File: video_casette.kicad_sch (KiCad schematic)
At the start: 4 parts, among them Q2 1402D, Q3 1402D

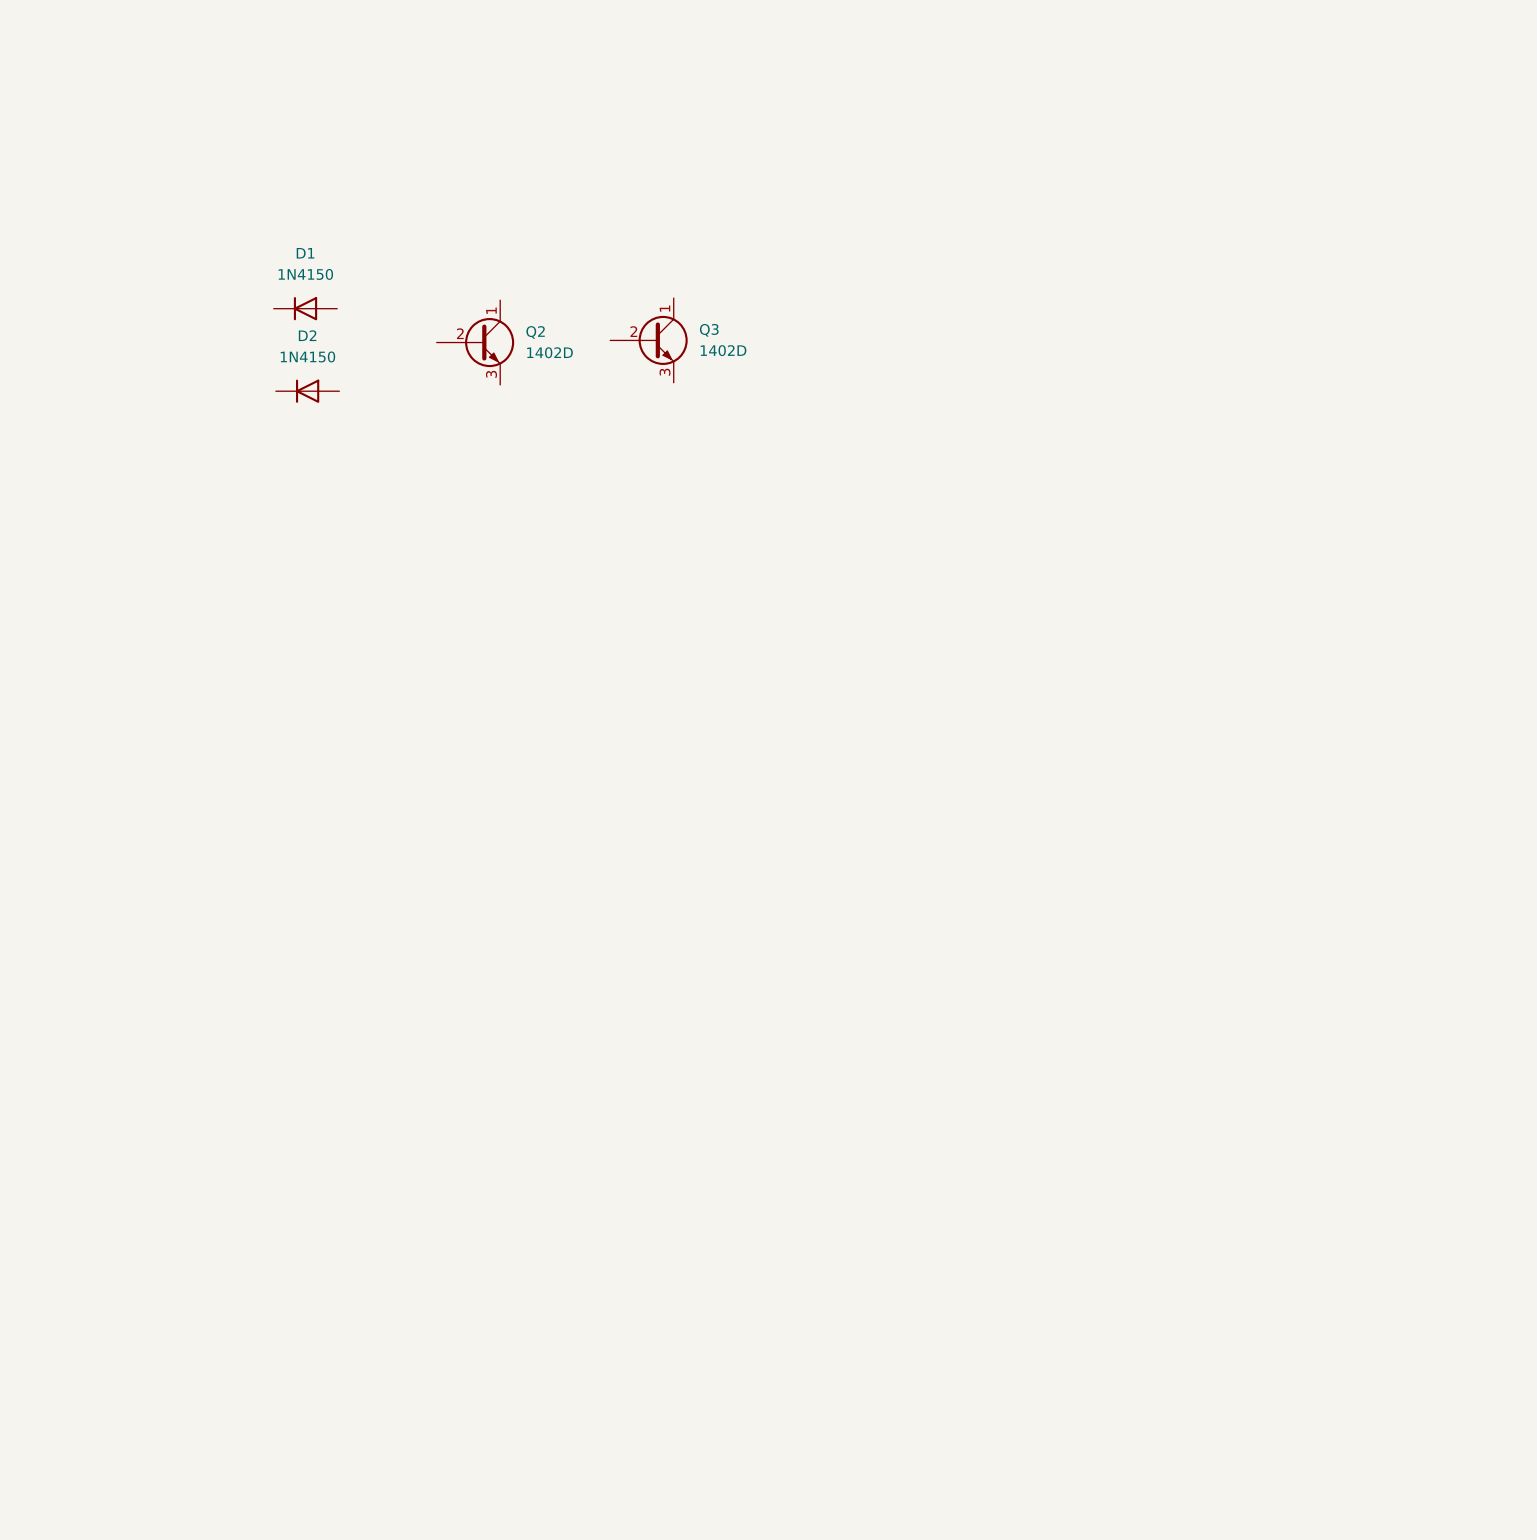
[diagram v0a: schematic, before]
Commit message: Finished Y-signal generation
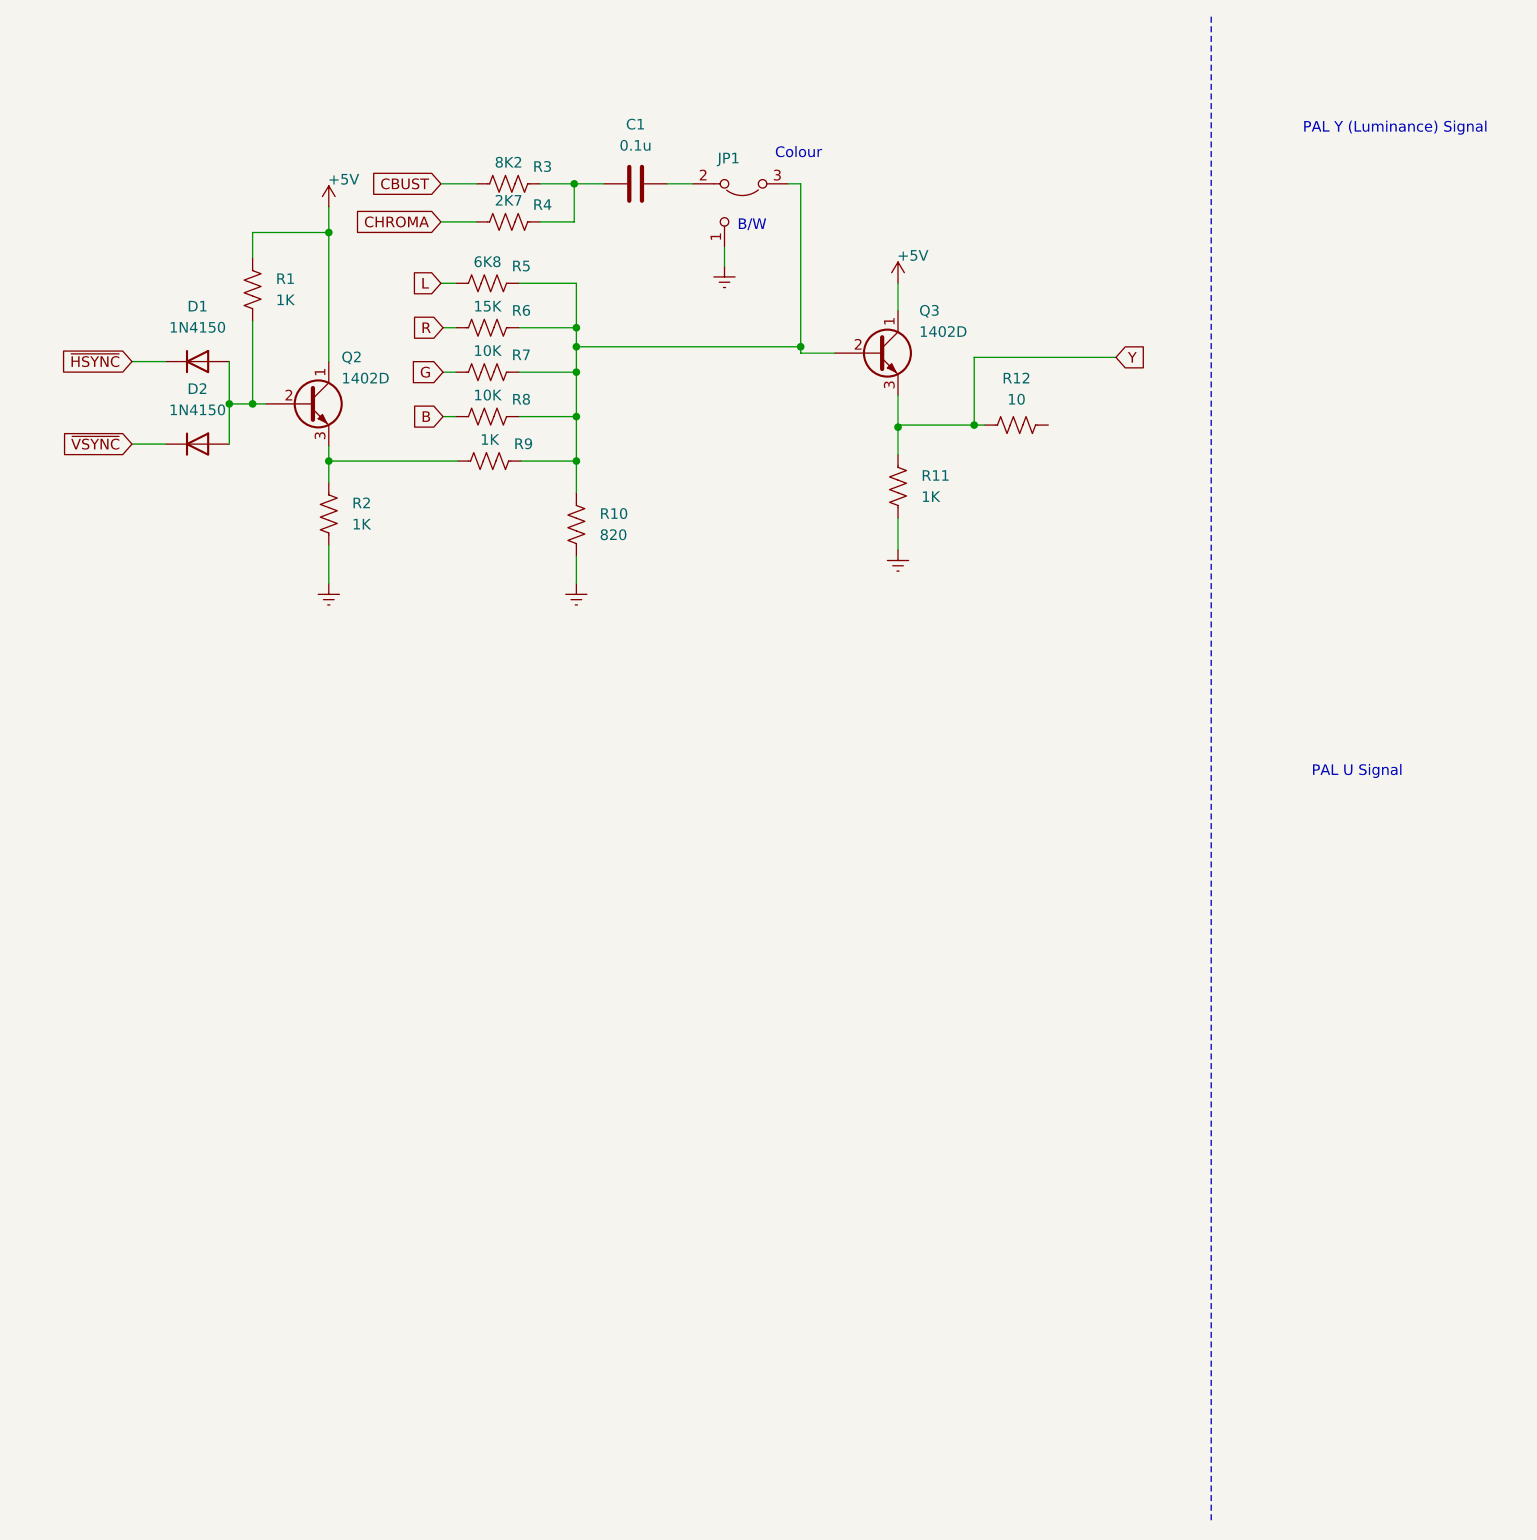
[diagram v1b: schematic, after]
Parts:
- added C1: 0.1u, symbol Device:C
- added JP1: Jumper 2-to-1_Bridged_23, symbol Laser500:Jumper 1-to-2
- added R1, R11, R2, R9: 1K, Resistor_THT:R_Axial_DIN0207_L6.3mm_D2.5mm_P7.62mm_Horizontal, symbol Device:R_US
- added R10: 820, Resistor_THT:R_Axial_DIN0207_L6.3mm_D2.5mm_P7.62mm_Horizontal, symbol Device:R_US
- added R12: 10, Resistor_THT:R_Axial_DIN0207_L6.3mm_D2.5mm_P7.62mm_Horizontal, symbol Device:R_US
- added R3: 8K2, Resistor_THT:R_Axial_DIN0207_L6.3mm_D2.5mm_P7.62mm_Horizontal, symbol Device:R_US
- added R4: 2K7, Resistor_THT:R_Axial_DIN0207_L6.3mm_D2.5mm_P7.62mm_Horizontal, symbol Device:R_US
- added R5: 6K8, Resistor_THT:R_Axial_DIN0207_L6.3mm_D2.5mm_P7.62mm_Horizontal, symbol Device:R_US
- added R6: 15K, Resistor_THT:R_Axial_DIN0207_L6.3mm_D2.5mm_P7.62mm_Horizontal, symbol Device:R_US
- added R7, R8: 10K, Resistor_THT:R_Axial_DIN0207_L6.3mm_D2.5mm_P7.62mm_Horizontal, symbol Device:R_US
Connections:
- net ~{HSYNC}: now reaches D1.1 (K)
- net at D1.2 (A): now also D2.2 (A), Q2.2 (B), R1.2
- net +5V: now reaches Q3.1 (C)
- net +5V: now also Q2.1 (C), R1.1
- net at Q3.2 (B): now also JP1.3 (B), R10.1, R5.1, R6.1, R7.1, R8.1, R9.1
- net Y: now reaches Q3.3 (E)
- net Y: now also R11.1, R12.1
- net ~{VSYNC}: now reaches D2.1 (K)
- net at Q2.3 (E): now also R2.1, R9.2
- new net: C1.2, R3.1, R4.1
- new net: C1.1, JP1.2 (C)
- new net B: R8.2
- new net CBUST: R3.2
- new net CHROMA: R4.2
- new net G: R7.2
- new net L: R5.2
- new net R: R6.2
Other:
- note added: "B/W"
- note added: "Colour"
- note added: "PAL U Signal"
- note added: "PAL Y (Luminance) Signal"
- moved on the sheet: D1, D2, Q2, Q3

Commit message: End of vacation
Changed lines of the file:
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@@
-		)
-	)
-	(global_label "R"
-		(shape input)
-		(at 60.452 52.07 180)
-		(fields_autoplaced yes)
-		(effects
-			(font
-				(size 1.27 1.27)
-			)
-			(justify right)
-		)
-		(property "Intersheetrefs" "${INTERSHEET_REFS}"
-			(at 56.1968 52.07 0)
-			(effects
-				(font
-					(size 1.27 1.27)
-				)
-				(justify right)
-				(hide yes)
-			)
 		)
 	)
@@
 		)
 	)
-	(global_label "B"
-		(shape input)
-		(at 60.452 62.738 180)
-		(fields_autoplaced yes)
-		(effects
-			(font
-				(size 1.27 1.27)
-			)
-			(justify right)
-		)
-		(property "Intersheetrefs" "${INTERSHEET_REFS}"
-			(at 56.1968 62.738 0)
-			(effects
-				(font
-					(size 1.27 1.27)
-				)
-				(justify right)
-				(hide yes)
-			)
-		)
-	)
-	(global_label "G"
-		(shape input)
-		(at 60.452 57.404 180)
-		(fields_autoplaced yes)
-		(effects
-			(font
-				(size 1.27 1.27)
-			)
-			(justify right)
-		)
-		(property "Intersheetrefs" "${INTERSHEET_REFS}"
-			(at 56.1968 57.404 0)
-			(effects
-				(font
-					(size 1.27 1.27)
-				)
-				(justify right)
-				(hide yes)
-			)
-		)
-	)
 	(global_label "~{HSYNC}"
 		(shape input)
@@
 		(property "Intersheetrefs" "${INTERSHEET_REFS}"
 			(at 13.8997 56.134 0)
-			(effects
-				(font
-					(size 1.27 1.27)
-				)
-				(justify right)
-				(hide yes)
-			)
-		)
-	)
-	(global_label "L"
-		(shape input)
-		(at 60.198 46.736 180)
-		(fields_autoplaced yes)
-		(effects
-			(font
-				(size 1.27 1.27)
-			)
-			(justify right)
-		)
-		(property "Intersheetrefs" "${INTERSHEET_REFS}"
-			(at 56.1847 46.736 0)
 			(effects
 				(font
@@
 		)
 	)
+	(hierarchical_label "R"
+		(shape input)
+		(at 60.452 52.07 180)
+		(fields_autoplaced yes)
+		(effects
+			(font
+				(size 1.27 1.27)
+			)
+			(justify right)
+		)
+	)
+	(hierarchical_label "B"
+		(shape input)
+		(at 60.452 62.738 180)
+		(fields_autoplaced yes)
+		(effects
+			(font
+				(size 1.27 1.27)
+			)
+			(justify right)
+		)
+	)
+	(hierarchical_label "G"
+		(shape input)
+		(at 60.452 57.404 180)
+		(fields_autoplaced yes)
+		(effects
+			(font
+				(size 1.27 1.27)
+			)
+			(justify right)
+		)
+	)
+	(hierarchical_label "L"
+		(shape input)
+		(at 60.198 46.736 180)
+		(fields_autoplaced yes)
+		(effects
+			(font
+				(size 1.27 1.27)
+			)
+			(justify right)
+		)
+	)

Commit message: More updates on Top and Main diagrams
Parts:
- added R??: 10K, Resistor_THT:R_Axial_DIN0207_L6.3mm_D2.5mm_P7.62mm_Horizontal, symbol Device:R_US
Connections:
- new net CASOUT: R??.2
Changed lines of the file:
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@@
+	(wire
+		(pts
+			(xy 34.29 111.76) (xy 41.91 111.76)
+		)
+		(stroke
+			(width 0)
+			(type default)
+		)
+	)
 	(wire
 		(pts
@@
 		)
 	)
-	(global_label "~{VSYNC}"
+	(global_label "Y"
 		(shape input)
-		(at 23.114 66.04 180)
+		(at 141.224 55.626 0)
 		(fields_autoplaced yes)
 		(effects
@@
 				(size 1.27 1.27)
 			)
-			(justify right)
+			(justify left)
 		)
 		(property "Intersheetrefs" "${INTERSHEET_REFS}"
-			(at 14.1416 66.04 0)
-			(effects
-				(font
-					(size 1.27 1.27)
-				)
-				(justify right)
-				(hide yes)
-			)
-		)
-	)
-	(global_label "CHROMA"
+			(at 145.2978 55.626 0)
+			(effects
+				(font
+					(size 1.27 1.27)
+				)
+				(justify left)
+				(hide yes)
+			)
+		)
+	)
+	(hierarchical_label "R"
 		(shape input)
-		(at 60.198 39.37 180)
+		(at 60.452 52.07 180)
 		(fields_autoplaced yes)
 		(effects
@@
 			(justify right)
 		)
-		(property "Intersheetrefs" "${INTERSHEET_REFS}"
-			(at 49.4718 39.37 0)
-			(effects
-				(font
-					(size 1.27 1.27)
-				)
-				(justify right)
-				(hide yes)
-			)
-		)
-	)
-	(global_label "~{HSYNC}"
+	)
+	(hierarchical_label "B"
 		(shape input)
-		(at 23.114 56.134 180)
+		(at 60.452 62.738 180)
 		(fields_autoplaced yes)
 		(effects
@@
 			(justify right)
 		)
-		(property "Intersheetrefs" "${INTERSHEET_REFS}"
-			(at 13.8997 56.134 0)
-			(effects
-				(font
-					(size 1.27 1.27)
-				)
-				(justify right)
-				(hide yes)
-			)
-		)
-	)
-	(global_label "CBUST"
+	)
+	(hierarchical_label "~{HSYNC}"
 		(shape input)
-		(at 60.198 34.798 180)
+		(at 23.114 56.134 180)
 		(fields_autoplaced yes)
 		(effects
@@
 			(justify right)
 		)
-		(property "Intersheetrefs" "${INTERSHEET_REFS}"
-			(at 51.1652 34.798 0)
-			(effects
-				(font
-					(size 1.27 1.27)
-				)
-				(justify right)
-				(hide yes)
-			)
-		)
-	)
-	(global_label "Y"
+	)
+	(hierarchical_label "~{VSYNC}"
 		(shape input)
-		(at 141.224 55.626 0)
+		(at 23.114 66.04 180)
 		(fields_autoplaced yes)
 		(effects
@@
 				(size 1.27 1.27)
 			)
-			(justify left)
-		)
-		(property "Intersheetrefs" "${INTERSHEET_REFS}"
-			(at 145.2978 55.626 0)
-			(effects
-				(font
-					(size 1.27 1.27)
-				)
-				(justify left)
-				(hide yes)
-			)
-		)
-	)
-	(hierarchical_label "R"
+			(justify right)
+		)
+	)
+	(hierarchical_label "G"
 		(shape input)
-		(at 60.452 52.07 180)
+		(at 60.452 57.404 180)
 		(fields_autoplaced yes)
 		(effects
@@
 		)
 	)
-	(hierarchical_label "B"
+	(hierarchical_label "L"
 		(shape input)
-		(at 60.452 62.738 180)
+		(at 60.198 46.736 180)
 		(fields_autoplaced yes)
 		(effects
@@
 		)
 	)
-	(hierarchical_label "G"
+	(hierarchical_label "CHROMA"
 		(shape input)
-		(at 60.452 57.404 180)
+		(at 60.198 39.37 180)
 		(fields_autoplaced yes)
 		(effects
@@
 		)
 	)
-	(hierarchical_label "L"
+	(hierarchical_label "CASOUT"
 		(shape input)
-		(at 60.198 46.736 180)
+		(at 34.29 111.76 180)
+		(fields_autoplaced yes)
+		(effects
+			(font
+				(size 1.27 1.27)
+			)
+			(justify right)
+		)
+	)
+	(hierarchical_label "CBUST"
+		(shape input)
+		(at 60.198 34.798 180)
 		(fields_autoplaced yes)
 		(effects
@@
 					(unit 1)
 				)
+			)
+		)
+	)
+	(symbol
+		(lib_id "Device:R_US")
+		(at 45.72 111.76 270)
+		(unit 1)
+		(exclude_from_sim no)
+		(in_bom yes)
+		(on_board yes)
+		(dnp no)
+		(fields_autoplaced yes)
+		(property "Reference" "R??"
+			(at 45.72 105.41 90)
+			(effects
+				(font
+					(size 1.27 1.27)
+				)
+			)
+		)
+		(property "Value" "10K"
+			(at 45.72 107.95 90)
+			(effects
+				(font
+					(size 1.27 1.27)
+				)
+			)
+		)
+		(property "Footprint" "Resistor_THT:R_Axial_DIN0207_L6.3mm_D2.5mm_P7.62mm_Horizontal"
+			(at 45.466 112.776 90)
+			(effects
+				(font
+					(size 1.27 1.27)
+				)
+				(hide yes)
+			)
+		)
+		(property "Datasheet" "~"
+			(at 45.72 111.76 0)
+			(effects
+				(font
+					(size 1.27 1.27)
+				)
+				(hide yes)
+			)
+		)
+		(property "Description" "Resistor, US symbol"
+			(at 45.72 111.76 0)
+			(effects
+				(font
+					(size 1.27 1.27)
+				)
+				(hide yes)
+			)
+		)
+		(pin "1"
+		)
+		(pin "2"
+		)
+		(instances
+			(project "Laser-500"
+				(path "/c1a6b1ae-77c2-4767-93cc-3749547878e9/8859e5dc-f590-4271-a1d5-ff92c9741b95"
+					(reference "R??")
+					(unit 1)
+				)
